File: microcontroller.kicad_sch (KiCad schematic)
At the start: 20 parts, among them J10 ESP_Only, J11 ESP32 [R], J12 SPI_EXPANSION, J13 I2C_EXPANSION, J16 ESP32 [L], J24 RPi Zero 2 W, J8 SHARED, J9 RPi_Only

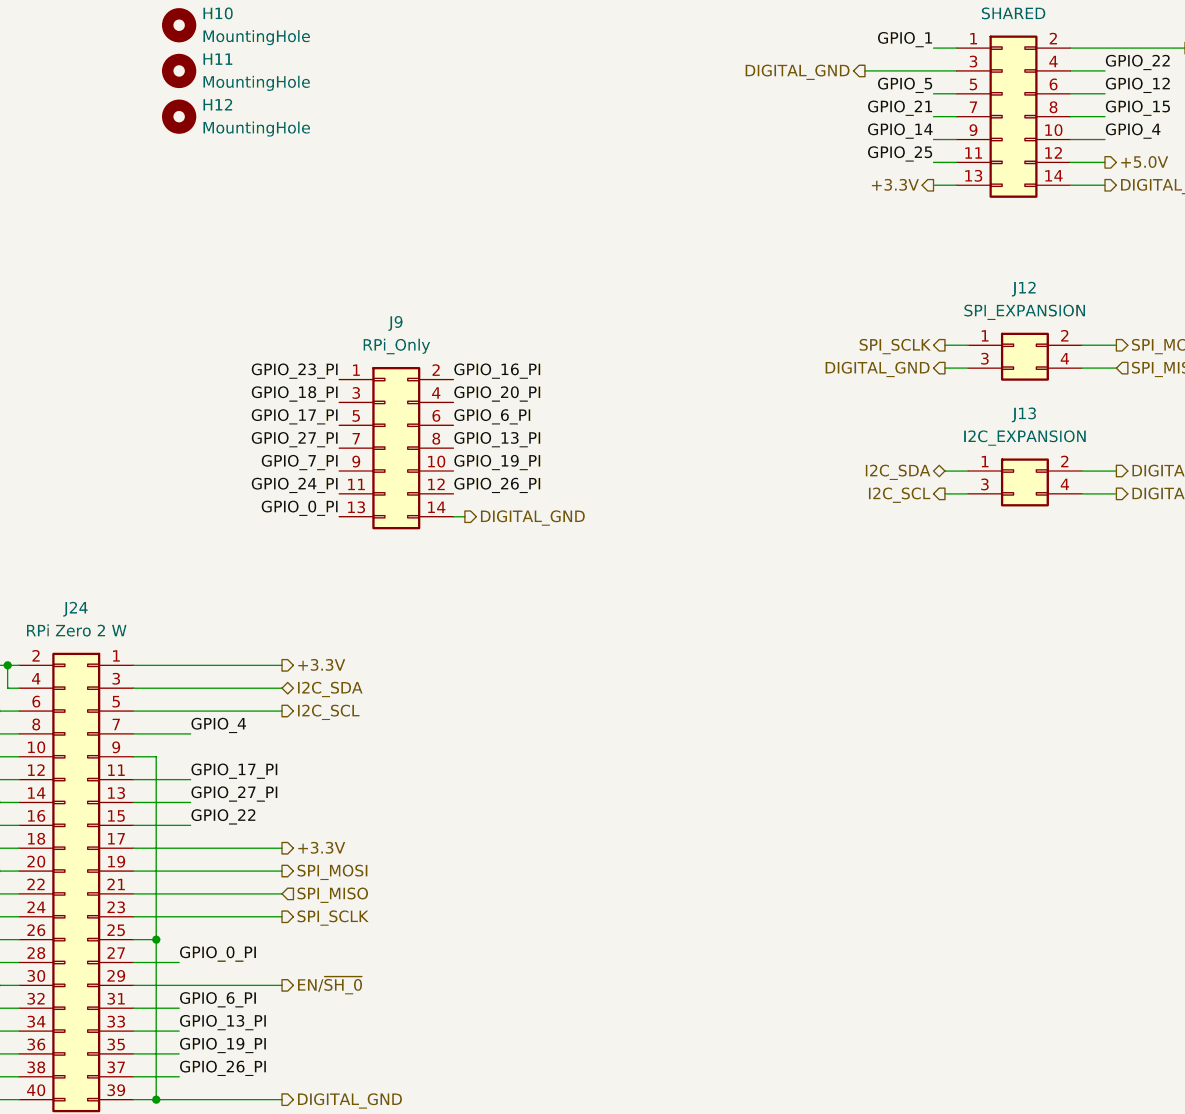
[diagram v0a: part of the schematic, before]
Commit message: Added board mounting holes, basic dimensions, and a board pdf file for casual viewing.
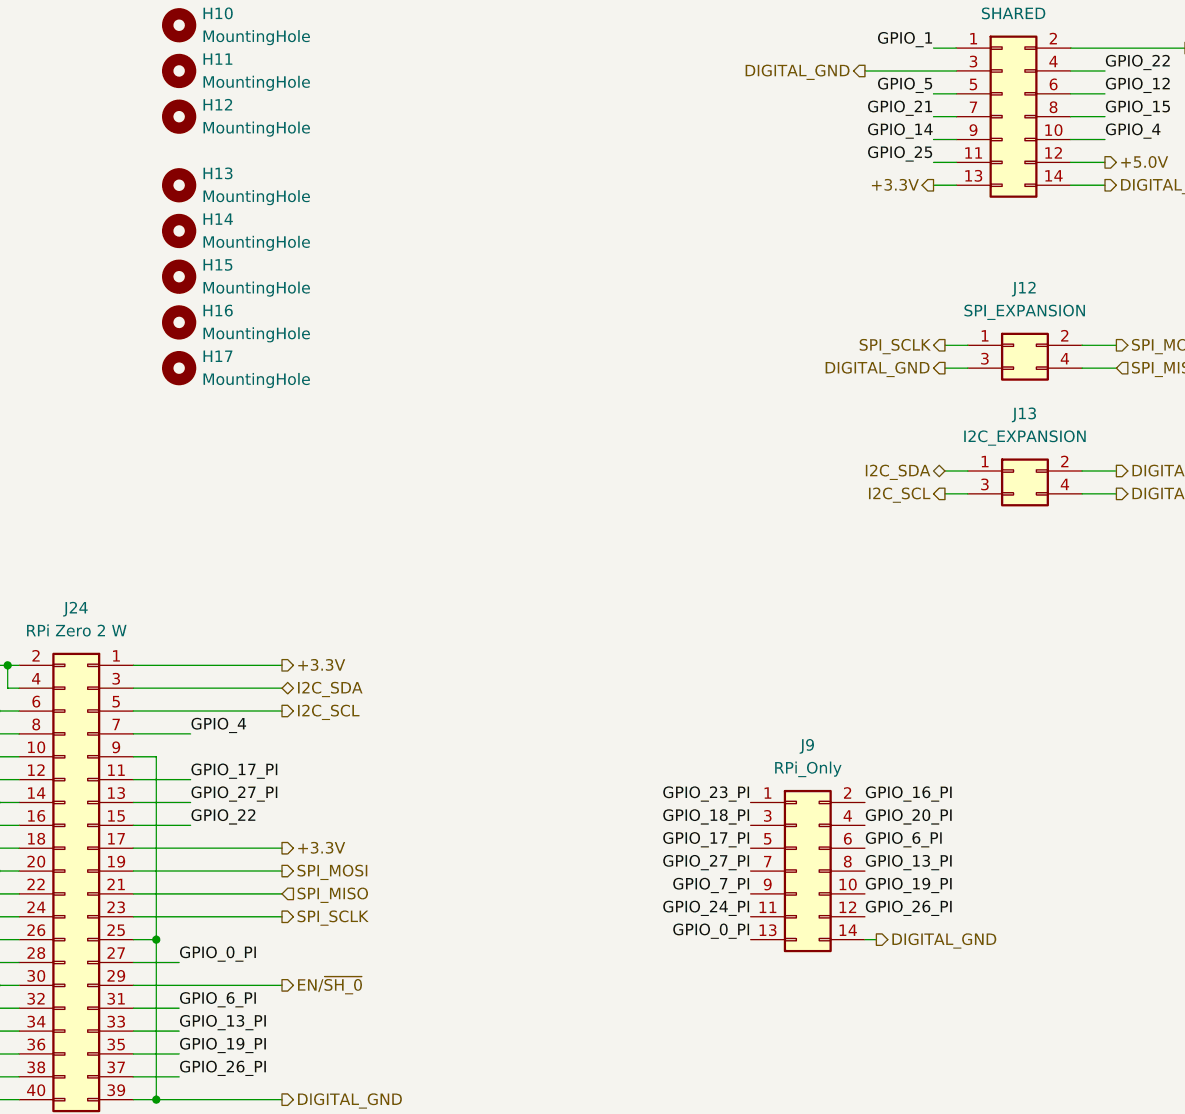
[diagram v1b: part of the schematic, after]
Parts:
- added H13, H14, H15, H16, H17: MountingHole, MountingHole:MountingHole_2.7mm_M2.5_ISO14580, symbol Mechanical:MountingHole
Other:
- moved on the sheet: J9
